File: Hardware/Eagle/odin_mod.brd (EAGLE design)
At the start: 21.4 x 22.8 mm, 36 parts

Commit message: Optimizations.
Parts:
- R9: value 47k -> 68k
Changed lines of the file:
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@@
 <element name="LIGHTOUT" library="wirepad" package="SMD1,27-2,54" value="1" x="20.2438" y="12.2682"/>
 <element name="TRIM" library="wirepad" package="SMD1,27-2,54" value="1" x="10.7442" y="21.844" rot="R90"/>
-<element name="R9" library="resistor" package="R0402" value="47k" x="20.6756" y="18.034" rot="R270"/>
+<element name="R9" library="resistor" package="R0402" value="68k" x="20.6756" y="18.034" rot="R270"/>
 </elements>
 <signals>
@@
 <contactref element="U$1" pad="22"/>
 <contactref element="U$3" pad="P$9_KATHODE_10_MIN"/>
-<wire x1="7.62" y1="8.4074" x2="7.0104" y2="8.4074" width="0.2032" layer="1"/>
-<wire x1="1.6256" y1="12.9032" x2="1.6256" y2="15.6718" width="0.2032" layer="1"/>
-<wire x1="7.0104" y1="8.4074" x2="6.9342" y2="8.6868" width="0.2032" layer="1"/>
-<wire x1="6.9342" y1="8.6868" x2="5.715" y2="9.906" width="0.2032" layer="1"/>
-<wire x1="5.715" y1="9.906" x2="5.715" y2="12.4206" width="0.2032" layer="1"/>
-<wire x1="1.6256" y1="12.9032" x2="5.0546" y2="12.9032" width="0.2032" layer="1"/>
-<wire x1="5.0546" y1="12.9032" x2="5.715" y2="12.4206" width="0.2032" layer="1"/>
-<wire x1="1.6256" y1="15.6718" x2="1.9558" y2="16.0528" width="0.2032" layer="1"/>
-<wire x1="1.9558" y1="16.0528" x2="2.96545" y2="16.0528" width="0.2032" layer="1"/>
+<wire x1="7.62" y1="8.4074" x2="7.0104" y2="8.4074" width="0.254" layer="1"/>
+<wire x1="1.6256" y1="12.9032" x2="1.6256" y2="15.6718" width="0.254" layer="1"/>
+<wire x1="7.0104" y1="8.4074" x2="6.9342" y2="8.6868" width="0.254" layer="1"/>
+<wire x1="6.9342" y1="8.6868" x2="5.715" y2="9.906" width="0.254" layer="1"/>
+<wire x1="5.715" y1="9.906" x2="5.715" y2="12.4206" width="0.254" layer="1"/>
+<wire x1="1.6256" y1="12.9032" x2="5.0546" y2="12.9032" width="0.254" layer="1"/>
+<wire x1="5.0546" y1="12.9032" x2="5.715" y2="12.4206" width="0.254" layer="1"/>
+<wire x1="1.6256" y1="15.6718" x2="1.9558" y2="16.0528" width="0.254" layer="1"/>
+<wire x1="1.9558" y1="16.0528" x2="2.96545" y2="16.0528" width="0.254" layer="1"/>
 <wire x1="2.96545" y1="16.0528" x2="2.9718" y2="16.04645" width="0.1524" layer="1"/>
 </signal>
@@
 <contactref element="U$1" pad="19"/>
 <contactref element="U$3" pad="P$10_KATHODE_1_HOUR"/>
-<wire x1="9.8552" y1="10.4394" x2="7.2136" y2="13.5636" width="0.2032" layer="1"/>
-<wire x1="10.0076" y1="9.4996" x2="9.8552" y2="10.4394" width="0.2032" layer="1"/>
-<wire x1="7.2136" y1="13.5636" x2="3.683" y2="13.5636" width="0.2032" layer="1"/>
+<wire x1="9.906" y1="10.4394" x2="7.2136" y2="13.5636" width="0.254" layer="1"/>
+<wire x1="10.0076" y1="9.4996" x2="9.906" y2="10.4394" width="0.254" layer="1"/>
+<wire x1="7.2136" y1="13.5636" x2="3.683" y2="13.5636" width="0.254" layer="1"/>
 <wire x1="3.683" y1="13.5636" x2="2.81305" y2="13.92555" width="0.2032" layer="1"/>
 </signal>

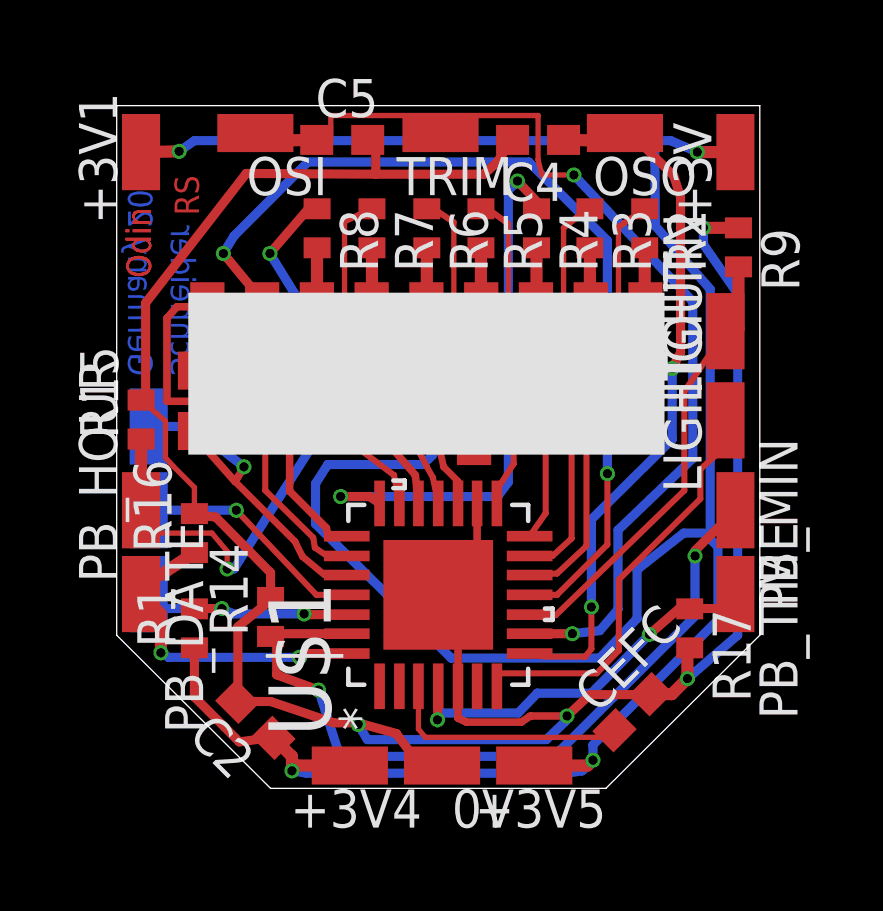
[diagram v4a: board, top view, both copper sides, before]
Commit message: Released ODIN MkII featuring n-mos transistors for the common cathodes.
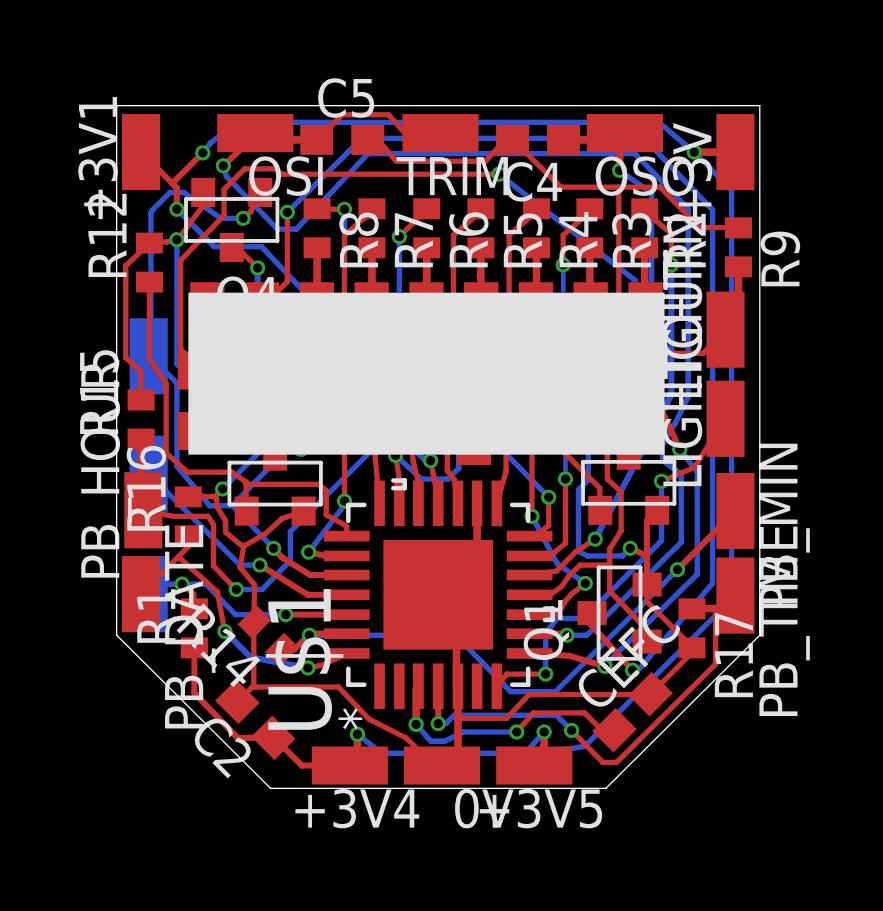
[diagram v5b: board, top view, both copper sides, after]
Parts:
- added Q1, Q2, Q3, Q4: IRLML0030, irlml0030:SOT-23
- added R10, R11, R12, R13: 47k, resistor:R0402
- moved PAD1 2.34 mm to (1.02, 14.4)
- moved PAD2 1.22 mm to (1.02, 10.5)
- moved R14 0.64 mm to (5.00, 5.08), turned to 135 degrees
- moved R16 0.59 mm to (2.34, 9.07)
- moved R17 0.08 mm to (19.1, 5.33)
- moved PB_HOUR 0.08 mm to (0.84, 9.27)
- moved LIGHTIN 0.05 mm to (20.2, 15.3)
- moved LIGHTOUT 0.05 mm to (20.2, 12.3)
- moved PB_TIME 0.05 mm to (20.6, 6.43)
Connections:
- new net N$11: Q4.P3, U$3.P$11_KATHODE_10_HOUR
- new net N$12: Q3.P3, U$3.P$10_KATHODE_1_HOUR
- new net N$13: Q2.P3, U$3.P$9_KATHODE_10_MIN
- new net N$14: Q1.P3, U$3.P$8_KATHODE_1_MIN
- net GND: now also Q1.P2, Q2.P2, Q3.P2, Q4.P2, R10.2, R11.2, R12.2, R13.2
- net PGC/LED_M7: now also Q4.P1, R10.1; no longer U$3.P$11_KATHODE_10_HOUR
- net RB1/LED_M6: now also Q3.P1, R11.1; no longer U$3.P$10_KATHODE_1_HOUR
- net RB4/LED_H4: now also Q2.P1, R12.1; no longer U$3.P$9_KATHODE_10_MIN
- net RC3/LED_M4: now also Q1.P1, R13.1; no longer U$3.P$8_KATHODE_1_MIN
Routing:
- net N$14: track 0.00 -> 38.6 mm, vias 0 -> 2
- net N$12: track 0.00 -> 28.1 mm, vias 0 -> 2
- net RC3/LED_M4: track 30.9 -> 12.9 mm, vias 2 -> 0
- net PGC/LED_M7: track 11.4 -> 26.5 mm, vias 1 -> 3
- net VDD: track 91.5 -> 77.9 mm, vias 5 -> 6
- net GND: track 83.3 -> 96.7 mm, vias 4 -> 5
- net T1OSI: track 34.6 -> 44.8 mm
- net N$11: track 0.00 -> 7.73 mm, vias 0 -> 2
- net RB3/LED_H3: track 19.3 -> 12.8 mm, vias 2 -> 0
- net RA0/SW1: track 25.7 -> 19.9 mm
- net N$13: track 0.00 -> 5.62 mm
- net N$1: track 15.5 -> 19.8 mm, vias 0 -> 4
- net RA5/SW4: track 12.8 -> 16.1 mm
- net RB5/LED_H1: track 16.4 -> 13.5 mm
- net RB2/LED_H2: track 12.5 -> 15.2 mm
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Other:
- board text removed: "Odin"
- board text removed: "RS"
- board text removed: "Roy Schneider Germany 2021"

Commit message: Updated image files.
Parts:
- R9: value 68k -> 47k
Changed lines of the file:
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@@
 <layer number="17" name="Pads" color="2" fill="1" visible="yes" active="yes"/>
 <layer number="18" name="Vias" color="2" fill="1" visible="yes" active="yes"/>
-<layer number="19" name="Unrouted" color="6" fill="1" visible="no" active="yes"/>
-<layer number="20" name="Dimension" color="15" fill="1" visible="no" active="yes"/>
-<layer number="21" name="tPlace" color="7" fill="1" visible="no" active="yes"/>
-<layer number="22" name="bPlace" color="7" fill="1" visible="no" active="yes"/>
-<layer number="23" name="tOrigins" color="15" fill="1" visible="no" active="yes"/>
-<layer number="24" name="bOrigins" color="15" fill="1" visible="no" active="yes"/>
+<layer number="19" name="Unrouted" color="6" fill="1" visible="yes" active="yes"/>
+<layer number="20" name="Dimension" color="15" fill="1" visible="yes" active="yes"/>
+<layer number="21" name="tPlace" color="7" fill="1" visible="yes" active="yes"/>
+<layer number="22" name="bPlace" color="7" fill="1" visible="yes" active="yes"/>
+<layer number="23" name="tOrigins" color="15" fill="1" visible="yes" active="yes"/>
+<layer number="24" name="bOrigins" color="15" fill="1" visible="yes" active="yes"/>
 <layer number="25" name="tNames" color="7" fill="1" visible="no" active="yes"/>
 <layer number="26" name="bNames" color="7" fill="1" visible="no" active="yes"/>
@@
 <element name="LIGHTOUT" library="wirepad" package="SMD1,27-2,54" value="1" x="20.2438" y="12.319"/>
 <element name="TRIM" library="wirepad" package="SMD1,27-2,54" value="1" x="10.7442" y="21.844" rot="R90"/>
-<element name="R9" library="resistor" package="R0402" value="68k" x="20.6756" y="18.034" rot="R270"/>
+<element name="R9" library="resistor" package="R0402" value="47k" x="20.6756" y="18.034" rot="R270"/>
 <element name="Q1" library="irlml0030" package="SOT-23" value="IRLML0030" x="16.7132" y="5.842" rot="R90"/>
 <element name="Q2" library="irlml0030" package="SOT-23" value="IRLML0030" x="5.2324" y="10.16"/>
